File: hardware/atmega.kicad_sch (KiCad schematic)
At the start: 9 parts, among them J3 ICSP, U202 ATmega328-A, Y201 Crystal_GND2

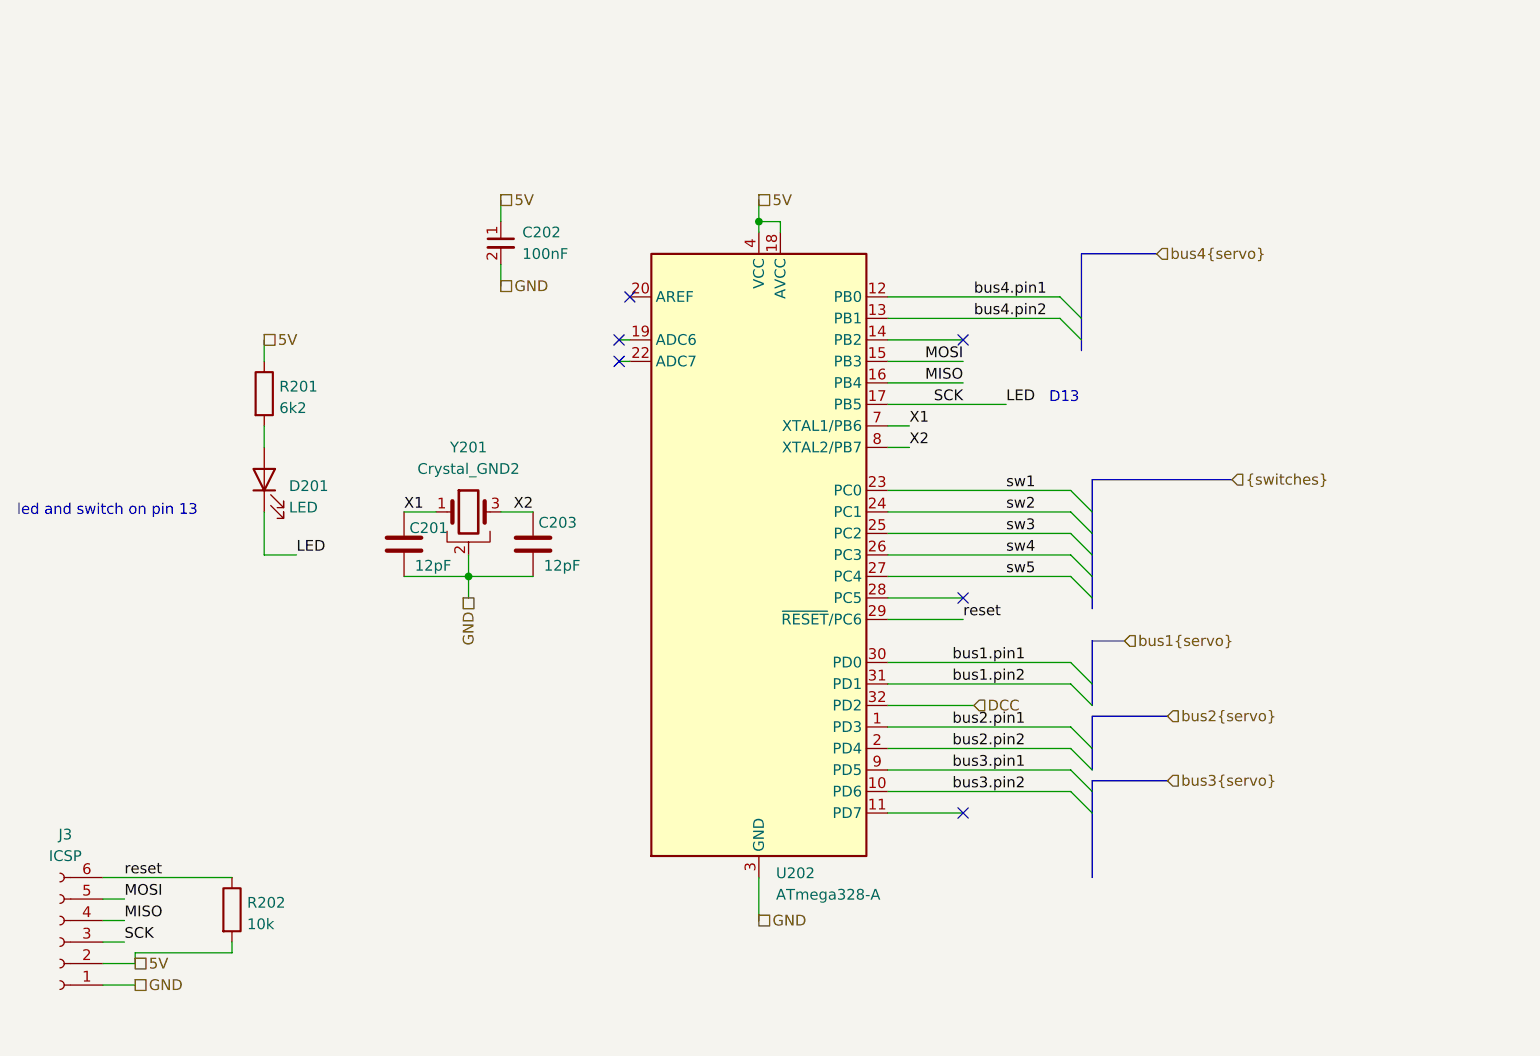
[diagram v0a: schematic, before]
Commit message: update board file, made similar to OS solenoid decoder
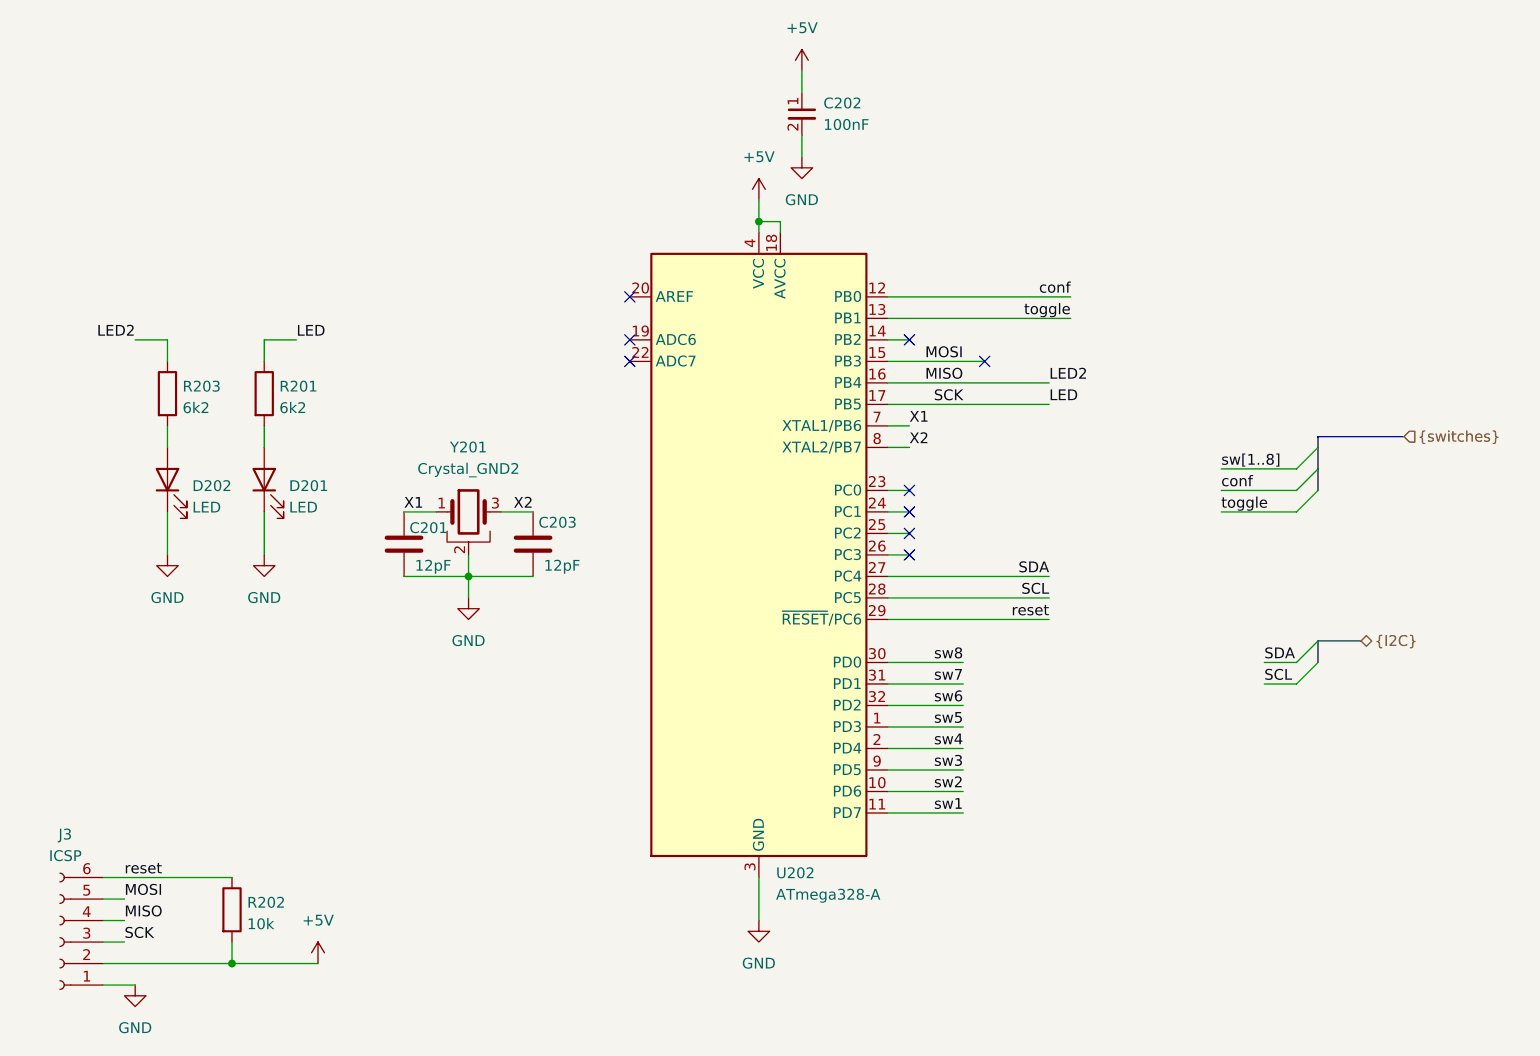
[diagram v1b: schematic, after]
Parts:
- added D202: LED, LED_SMD:LED_0805_2012Metric_Pad1.15x1.40mm_HandSolder, symbol Device:LED
- added R203: 6k2, Resistor_SMD:R_0603_1608Metric_Pad0.98x0.95mm_HandSolder, symbol Device:R
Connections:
- net bus2.pin1 is gone; now on net sw5: U202.1 (PD3)
- net bus2.pin2 is gone; now on net sw4: U202.2 (PD4)
- net bus3.pin1 is gone; now on net sw3: U202.9 (PD5)
- net bus3.pin2 is gone; now on net sw2: U202.10 (PD6)
- net GND: now also D201.1 (K), D202.1 (K)
- net LED: now also R201.1; no longer D201.1 (K)
- net sw1: now also U202.11 (PD7); no longer U202.23 (PC0)
- net sw2: no longer U202.24 (PC1)
- net sw3: no longer U202.25 (PC2)
- net sw4: no longer U202.26 (PC3)
- net sw5: no longer U202.27 (PC4)
- net SCL: now reaches U202.28 (PC5)
- net 5V renamed +5V
- net +5V: no longer R201.1
- net DCC renamed sw6
- net MISO renamed LED2
- net LED2: now also R203.1
- net bus1.pin1 renamed sw8
- net bus1.pin2 renamed sw7
- net bus4.pin1 renamed conf
- net bus4.pin2 renamed toggle
- new net: D202.2 (A), R203.2
- new net SDA: U202.27 (PC4)
- no-connect marks 6 -> 9
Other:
- note removed: "D13"
- note removed: "led and switch on pin 13"
- moved on the sheet: C202

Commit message: added manual and picture
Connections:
- net sw6: now also U202.26 (PC3); no longer U202.32 (PD2)
- new net DCC: U202.32 (PD2)
- no-connect marks 9 -> 7
